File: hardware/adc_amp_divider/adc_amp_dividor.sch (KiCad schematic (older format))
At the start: 114 parts, among them M1 CONN_1, M2 CONN_1, M3 CONN_1, P1 CONN_10X2, P2 CONN_6, P3 CONN_6, P4 CONN_3, P5 CONN_2, P6 CONN_1, P7 CONN_1, U1 LMV324IDR, U2 LMV324IDR, U3 LMV324IDR

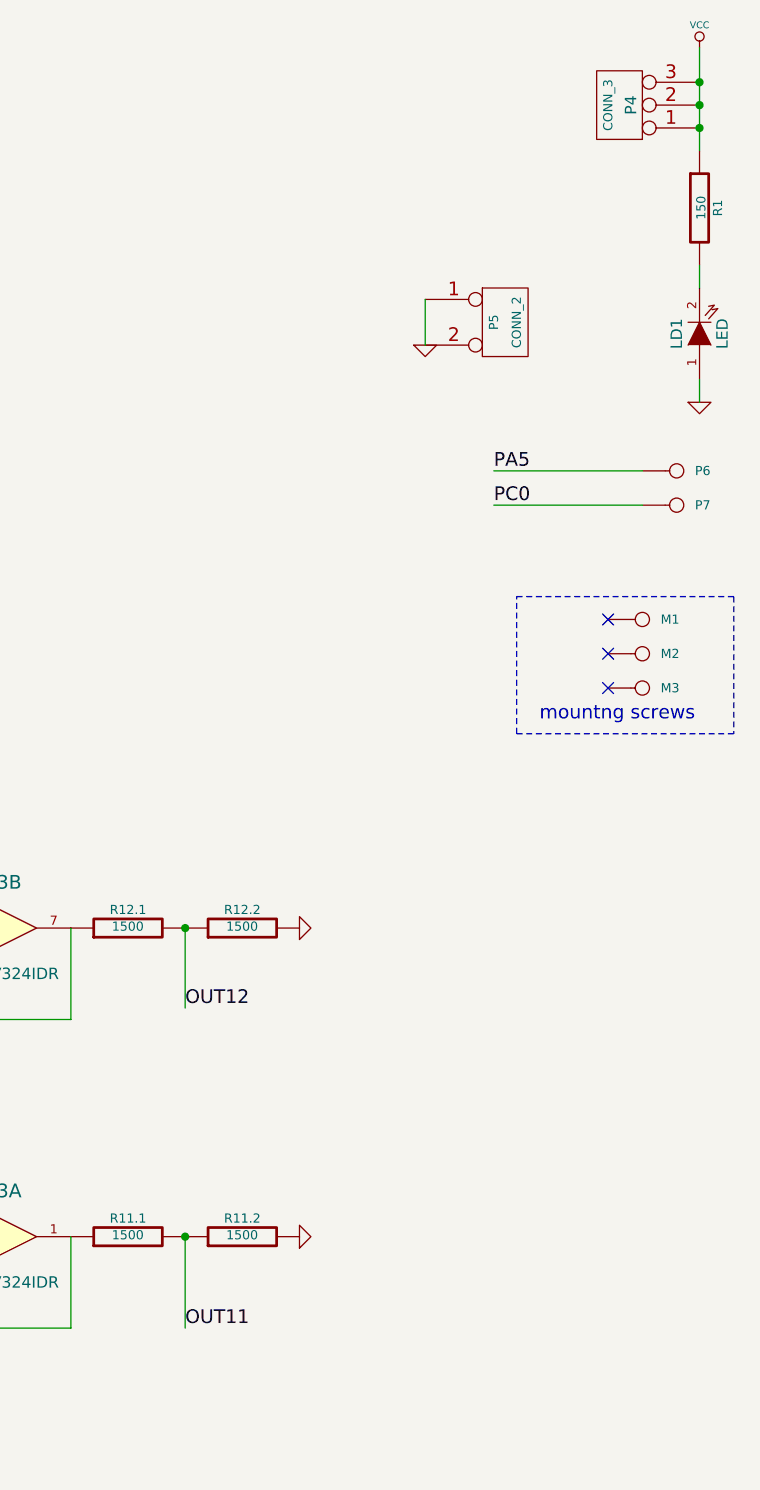
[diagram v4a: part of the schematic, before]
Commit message: 
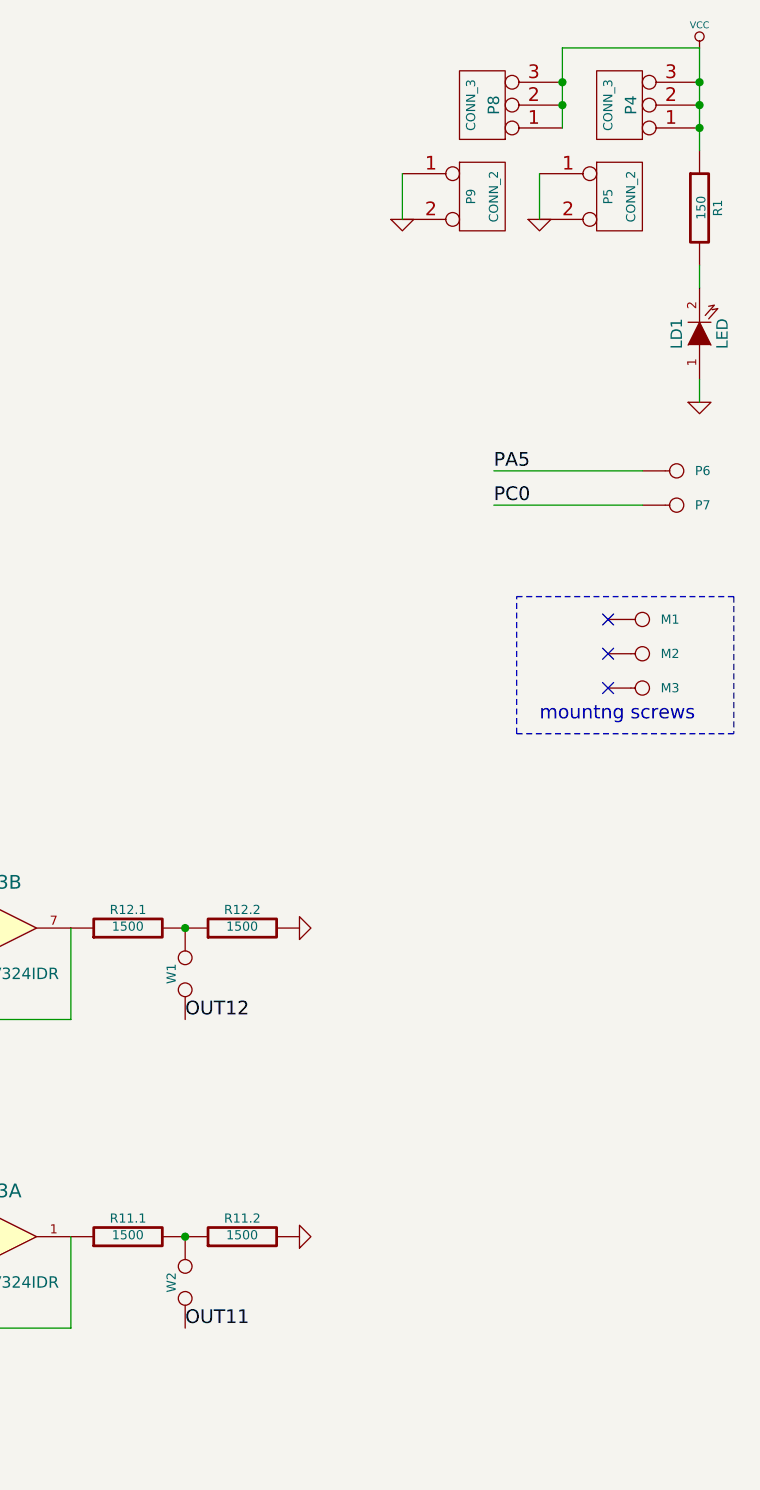
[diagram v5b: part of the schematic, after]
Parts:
- added P8: CONN_3, symbol CONN_3
- added P9: CONN_2, SIL-2, symbol CONN_2
- added W1, W2: TEST, SIL-2, symbol TEST
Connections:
- net GND: now also P9.1 (P201), P9.2 (PM)
- net OUT11: now also W2.1; no longer R11.1.2, R11.2.1
- net OUT12: now also W1.1; no longer R12.1.2, R12.2.1
- net VCC: now also P8.1 (P201), P8.2 (PM), P8.3 (P209)
- new net: R11.1.2, R11.2.1, W2.2
- new net: R12.1.2, R12.2.1, W1.2
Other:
- moved on the sheet: P5
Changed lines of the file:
@@
 Sheet 1 1
 Title "Analgo Protection board for RUSEFI.com"
-Date "27 nov 2013"
+Date "29 nov 2013"
 Rev "A-1"
 Comp "RUSEFI.com"
@@
 Text Label 13950 6250 0    60   ~ 0
 OUT11
-Text Label 13950 4850 0    60   ~ 0
+Text Label 13950 4900 0    60   ~ 0
 OUT12
 Text Label 10300 4400 0    60   ~ 0
@@
 	12350 5750 12750 5750
 Connection ~ 13950 4500
-Wire Wire Line
-	13950 4500 13950 4850
 Connection ~ 10650 4400
 Connection ~ 13950 5850
-Wire Wire Line
-	13950 5850 13950 6250
 Connection ~ 12350 5750
 Wire Wire Line
@@
 L CONN_2 P5
 U 1 1 5296836D
-P 15350 1850
-F 0 "P5" V 15300 1850 40  0000 C CNN
-F 1 "CONN_2" V 15400 1850 40  0000 C CNN
-F 2 "SIL-2" H 15350 1850 60  0001 C CNN
-F 3 "" H 15350 1850 60  0000 C CNN
-	1    15350 1850
+P 15850 1300
+F 0 "P5" V 15800 1300 40  0000 C CNN
+F 1 "CONN_2" V 15900 1300 40  0000 C CNN
+F 2 "SIL-2" H 15850 1300 60  0001 C CNN
+F 3 "" H 15850 1300 60  0000 C CNN
+	1    15850 1300
 	1    0    0    -1
 $EndComp
@@
 L GND #PWR089
 U 1 1 5296855D
-P 15000 1950
-F 0 "#PWR089" H 15000 1950 30  0001 C CNN
-F 1 "GND" H 15000 1880 30  0001 C CNN
-F 2 "" H 15000 1950 60  0000 C CNN
-F 3 "" H 15000 1950 60  0000 C CNN
-	1    15000 1950
-	1    0    0    -1
-$EndComp
-Wire Wire Line
-	15000 1950 15000 1750
+P 15500 1400
+F 0 "#PWR089" H 15500 1400 30  0001 C CNN
+F 1 "GND" H 15500 1330 30  0001 C CNN
+F 2 "" H 15500 1400 60  0000 C CNN
+F 3 "" H 15500 1400 60  0000 C CNN
+	1    15500 1400
+	1    0    0    -1
+$EndComp
+Wire Wire Line
+	15500 1400 15500 1200
+$Comp
+L CONN_3 P8
+U 1 1 5297E845
+P 15250 900
+F 0 "P8" V 15200 900 50  0000 C CNN
+F 1 "CONN_3" V 15300 900 40  0000 C CNN
+F 2 "" H 15250 900 60  0000 C CNN
+F 3 "" H 15250 900 60  0000 C CNN
+	1    15250 900
+	-1   0    0    1
+$EndComp
+Wire Wire Line
+	15600 650  15600 1000
+Connection ~ 15600 900
+Wire Wire Line
+	16200 650  15600 650
+Connection ~ 15600 800
+$Comp
+L CONN_2 P9
+U 1 1 5297EAA7
+P 15250 1300
+F 0 "P9" V 15200 1300 40  0000 C CNN
+F 1 "CONN_2" V 15300 1300 40  0000 C CNN
+F 2 "SIL-2" H 15250 1300 60  0001 C CNN
+F 3 "" H 15250 1300 60  0000 C CNN
+	1    15250 1300
+	1    0    0    -1
+$EndComp
+$Comp
+L GND #PWR090
+U 1 1 5297EAAD
+P 14900 1400
+F 0 "#PWR090" H 14900 1400 30  0001 C CNN
+F 1 "GND" H 14900 1330 30  0001 C CNN
+F 2 "" H 14900 1400 60  0000 C CNN
+F 3 "" H 14900 1400 60  0000 C CNN
+	1    14900 1400
+	1    0    0    -1
+$EndComp
+Wire Wire Line
+	14900 1400 14900 1200
+$Comp
+L TEST W1
+U 1 1 5298705E
+P 13950 4700
+F 0 "W1" H 13950 4760 40  0000 C CNN
+F 1 "TEST" H 13950 4630 40  0001 C CNN
+F 2 "SIL-2" H 13950 4700 60  0001 C CNN
+F 3 "" H 13950 4700 60  0000 C CNN
+	1    13950 4700
+	0    -1   -1   0
+$EndComp
+$Comp
+L TEST W2
+U 1 1 52987094
+P 13950 6050
+F 0 "W2" H 13950 6110 40  0000 C CNN
+F 1 "TEST" H 13950 5980 40  0001 C CNN
+F 2 "SIL-2" H 13950 6050 60  0001 C CNN
+F 3 "" H 13950 6050 60  0000 C CNN
+	1    13950 6050
+	0    -1   -1   0
+$EndComp
 $EndSCHEMATC

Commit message: seeed components
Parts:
- R1: value 150 -> 100
- R1.4, R10.4, R11.4, R12.4, R2.4, R3.4, R4.4, R5.4, R6.4, R7.4, R8.4, R9.4: value 150 -> 100; vend1,vend1# (none) -> seeed,0030110P1
- U1, U2, U3: vend1,vend1# (none) -> seeed,1100030P1
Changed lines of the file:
@@
 P 3100 8600
 F 0 "R1.4" V 3180 8600 40  0000 C CNN
-F 1 "150" V 3107 8601 40  0000 C CNN
+F 1 "100" V 3107 8601 40  0000 C CNN
 F 2 "~" V 3030 8600 30  0000 C CNN
 F 3 "~" H 3100 8600 30  0000 C CNN
+F 4 "seeed,0030110P1" V 3100 8600 60  0001 C CNN "vend1,vend1#"
 	1    3100 8600
 	0    -1   -1   0
@@
 P 3100 7100
 F 0 "R2.4" V 3180 7100 40  0000 C CNN
-F 1 "150" V 3107 7101 40  0000 C CNN
+F 1 "100" V 3107 7101 40  0000 C CNN
 F 2 "~" V 3030 7100 30  0000 C CNN
 F 3 "~" H 3100 7100 30  0000 C CNN
+F 4 "seeed,0030110P1" V 3100 7100 60  0001 C CNN "vend1,vend1#"
 	1    3100 7100
 	0    -1   -1   0
@@
 P 3450 5700
 F 0 "R3.4" V 3530 5700 40  0000 C CNN
-F 1 "150" V 3457 5701 40  0000 C CNN
+F 1 "100" V 3457 5701 40  0000 C CNN
 F 2 "~" V 3380 5700 30  0000 C CNN
 F 3 "~" H 3450 5700 30  0000 C CNN
+F 4 "seeed,0030110P1" V 3450 5700 60  0001 C CNN "vend1,vend1#"
 	1    3450 5700
 	0    -1   -1   0
@@
 P 3450 4500
 F 0 "R4.4" V 3530 4500 40  0000 C CNN
-F 1 "150" V 3457 4501 40  0000 C CNN
+F 1 "100" V 3457 4501 40  0000 C CNN
 F 2 "~" V 3380 4500 30  0000 C CNN
 F 3 "~" H 3450 4500 30  0000 C CNN
+F 4 "seeed,0030110P1" V 3450 4500 60  0001 C CNN "vend1,vend1#"
 	1    3450 4500
 	0    -1   -1   0
@@
 P 7750 5800
 F 0 "R7.4" V 7830 5800 40  0000 C CNN
-F 1 "150" V 7757 5801 40  0000 C CNN
+F 1 "100" V 7757 5801 40  0000 C CNN
 F 2 "~" V 7680 5800 30  0000 C CNN
 F 3 "~" H 7750 5800 30  0000 C CNN
+F 4 "seeed,0030110P1" V 7750 5800 60  0001 C CNN "vend1,vend1#"
 	1    7750 5800
 	0    -1   -1   0
@@
 P 7800 4450
 F 0 "R8.4" V 7880 4450 40  0000 C CNN
-F 1 "150" V 7807 4451 40  0000 C CNN
+F 1 "100" V 7807 4451 40  0000 C CNN
 F 2 "~" V 7730 4450 30  0000 C CNN
 F 3 "~" H 7800 4450 30  0000 C CNN
+F 4 "seeed,0030110P1" V 7800 4450 60  0001 C CNN "vend1,vend1#"
 	1    7800 4450
 	0    -1   -1   0
@@
 P 7700 8550
 F 0 "R5.4" V 7780 8550 40  0000 C CNN
-F 1 "150" V 7707 8551 40  0000 C CNN
+F 1 "100" V 7707 8551 40  0000 C CNN
 F 2 "~" V 7630 8550 30  0000 C CNN
 F 3 "~" H 7700 8550 30  0000 C CNN
+F 4 "seeed,0030110P1" V 7700 8550 60  0001 C CNN "vend1,vend1#"
 	1    7700 8550
 	0    -1   -1   0
@@
 P 7700 7200
 F 0 "R6.4" V 7780 7200 40  0000 C CNN
-F 1 "150" V 7707 7201 40  0000 C CNN
+F 1 "100" V 7707 7201 40  0000 C CNN
 F 2 "~" V 7630 7200 30  0000 C CNN
 F 3 "~" H 7700 7200 30  0000 C CNN
+F 4 "seeed,0030110P1" V 7700 7200 60  0001 C CNN "vend1,vend1#"
 	1    7700 7200
 	0    -1   -1   0
@@
 P 16200 1350
 F 0 "R1" V 16280 1350 40  0000 C CNN
-F 1 "150" V 16207 1351 40  0000 C CNN
+F 1 "100" V 16207 1351 40  0000 C CNN
 F 2 "~" V 16130 1350 30  0000 C CNN
 F 3 "~" H 16200 1350 30  0000 C CNN
@@
 P 12100 8650
 F 0 "R9.4" V 12180 8650 40  0000 C CNN
-F 1 "150" V 12107 8651 40  0000 C CNN
+F 1 "100" V 12107 8651 40  0000 C CNN
 F 2 "~" V 12030 8650 30  0000 C CNN
 F 3 "~" H 12100 8650 30  0000 C CNN
+F 4 "seeed,0030110P1" V 12100 8650 60  0001 C CNN "vend1,vend1#"
 	1    12100 8650
 	0    -1   -1   0
@@
 P 12150 7300
 F 0 "R10.4" V 12230 7300 40  0000 C CNN
-F 1 "150" V 12157 7301 40  0000 C CNN
+F 1 "100" V 12157 7301 40  0000 C CNN
 F 2 "~" V 12080 7300 30  0000 C CNN
 F 3 "~" H 12150 7300 30  0000 C CNN
+F 4 "seeed,0030110P1" V 12150 7300 60  0001 C CNN "vend1,vend1#"
 	1    12150 7300
 	0    -1   -1   0
@@
 F 2 "" H 4400 5800 60  0000 C CNN
 F 3 "" H 4400 5800 60  0000 C CNN
+F 4 "seeed,1100030P1" H 4400 5800 60  0001 C CNN "vend1,vend1#"
 	1    4400 5800
 	1    0    0    -1
@@
 F 2 "" H 8750 5900 60  0000 C CNN
 F 3 "" H 8750 5900 60  0000 C CNN
+F 4 "seeed,1100030P1" H 8750 5900 60  0001 C CNN "vend1,vend1#"
 	1    8750 5900
 	1    0    0    -1
@@
 P 12100 5750
 F 0 "R11.4" V 12180 5750 40  0000 C CNN
-F 1 "150" V 12107 5751 40  0000 C CNN
+F 1 "100" V 12107 5751 40  0000 C CNN
 F 2 "~" V 12030 5750 30  0000 C CNN
 F 3 "~" H 12100 5750 30  0000 C CNN
+F 4 "seeed,0030110P1" V 12100 5750 60  0001 C CNN "vend1,vend1#"
 	1    12100 5750
 	0    -1   -1   0
@@
 P 12150 4400
 F 0 "R12.4" V 12230 4400 40  0000 C CNN
-F 1 "150" V 12157 4401 40  0000 C CNN
+F 1 "100" V 12157 4401 40  0000 C CNN
 F 2 "~" V 12080 4400 30  0000 C CNN
 F 3 "~" H 12150 4400 30  0000 C CNN
+F 4 "seeed,0030110P1" V 12150 4400 60  0001 C CNN "vend1,vend1#"
 	1    12150 4400
 	0    -1   -1   0
@@
 F 2 "" H 13100 5850 60  0000 C CNN
 F 3 "" H 13100 5850 60  0000 C CNN
+F 4 "seeed,1100030P1" H 13100 5850 60  0001 C CNN "vend1,vend1#"
 	1    13100 5850
 	1    0    0    -1

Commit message: global rename
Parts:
- renumbered C1.1 to C210, C1.2 to C220, C2.1 to C220, C3.1 to C230, C4.1 to C240, C5.1 to C250, C5.2 to C251, C6.1 to C260, C7,1 to C270, C8.1 to C280, C9.1 to C290, C9.2 to C291, C10.1 to C300, C11.1 to C310, C12.1 to C320, D1 to D210, D2 to D220, D3 to D230, D4 to D240, D5 to D250, D6 to D260, D7 to D270, D8 to D280, D9 to D290, D10 to D300, D11 to D310, D12 to D320, LD1 to LD200, M1 to M200, M2 to M201, M3 to M202, P1 to P201, P4 to P202, P5 to P203, P6 to P204, P7 to P205, P8 to P206, P9 to P207, P2 to P208, P3 to P209, R1 to R200, R1.5 to R210, R1.2 to R220, R2.2 to R220, R2.5 to R220, R3.2 to R220, R4.2 to R220, R7.2 to R220, R5.2 to R220, R9.2 to R220, R1.6 to R220, R3.6 to R220, R4.6 to R220, R5.6 to R220, R9.6 to R220, R7.6 to R220, R2.3 to R221, R1.4 to R221, R3.4 to R221, R4.4 to R221, R7.4 to R221, R5.4 to R221, R9.4 to R221, R2.6 to R222, R1.1 to R223, R1.3 to R223, R2.1 to R223, R2.4 to R223, R3.1 to R223, R3.3 to R223, R4.3 to R223, R4.1 to R223, R7.1 to R223, R7.3 to R223, R5.1 to R223, R5.3 to R223, R9.1 to R223, R9.3 to R223, R3.5 to R230, R4.5 to R240, R5.5 to R250, R6.5 to R260, R6.3 to R261, R6.6 to R262, R6.4 to R263, R6.1 to R264, R6.2 to R265, R7.5 to R270, R8.5 to R280, R8.3 to R281, R8.6 to R282, R8.4 to R283, R8.1 to R284, R8.2 to R285, R9.5 to R290, R10.5 to R300, R10.3 to R301, R10.6 to R302, R10.4 to R303, R10.1 to R304, R10.2 to R305, R11.5 to R310, R11.3 to R311, R11.6 to R312, R11.4 to R313, R11.1 to R314, R11.2 to R315, R12.5 to R320, R12.3 to R321, R12.6 to R322, R12.4 to R323, R12.1 to R324, R12.2 to R325, U1 to U201, U2 to U202, U3 to U203, W2 to W211, W1 to W212
